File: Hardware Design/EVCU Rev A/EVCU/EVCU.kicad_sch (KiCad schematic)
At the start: 89 parts, among them J1 Conn_01x06, J2 Conn_01x02, J3 APPS/BSE_Conn, J4 Micro_SD_Card, J5 DB9_Male, J6 Conn_01x02, Q1 Q_PMOS_GSD, U1 AZ1117-3.3, U10 EMIF06-MSD02N16, U11 ESDALC6V1W5, U2 AP62250WU-7, U3 STM32L4R9ZITx, U4 LM358, U5 MPU-6500, U6 SN65HVD230, U7 LM358, U9 ESDCAN24-2BLY, X1 ECS-2520MV-160-CN-TR

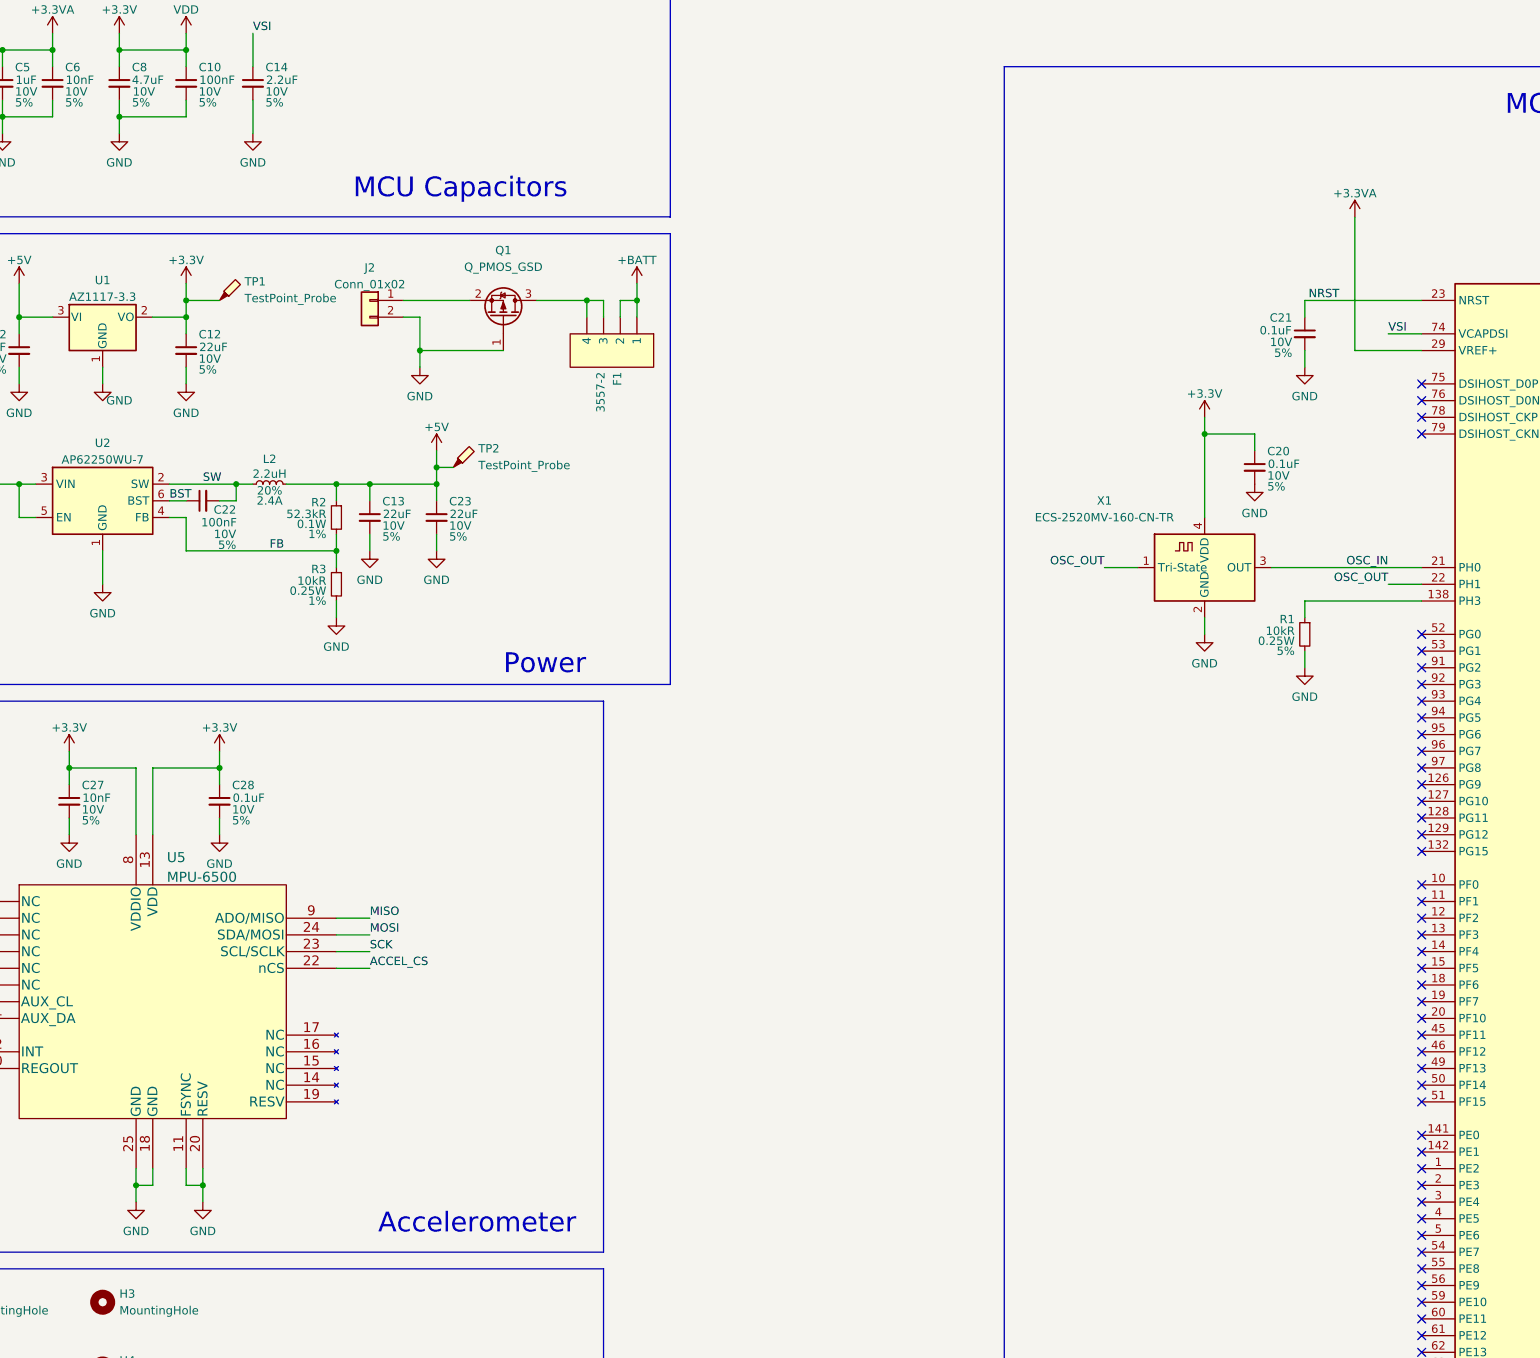
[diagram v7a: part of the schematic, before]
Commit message: added vref+ caps, fixed f1 via error, fixed gyro footprint, pcb ready for manufacturing
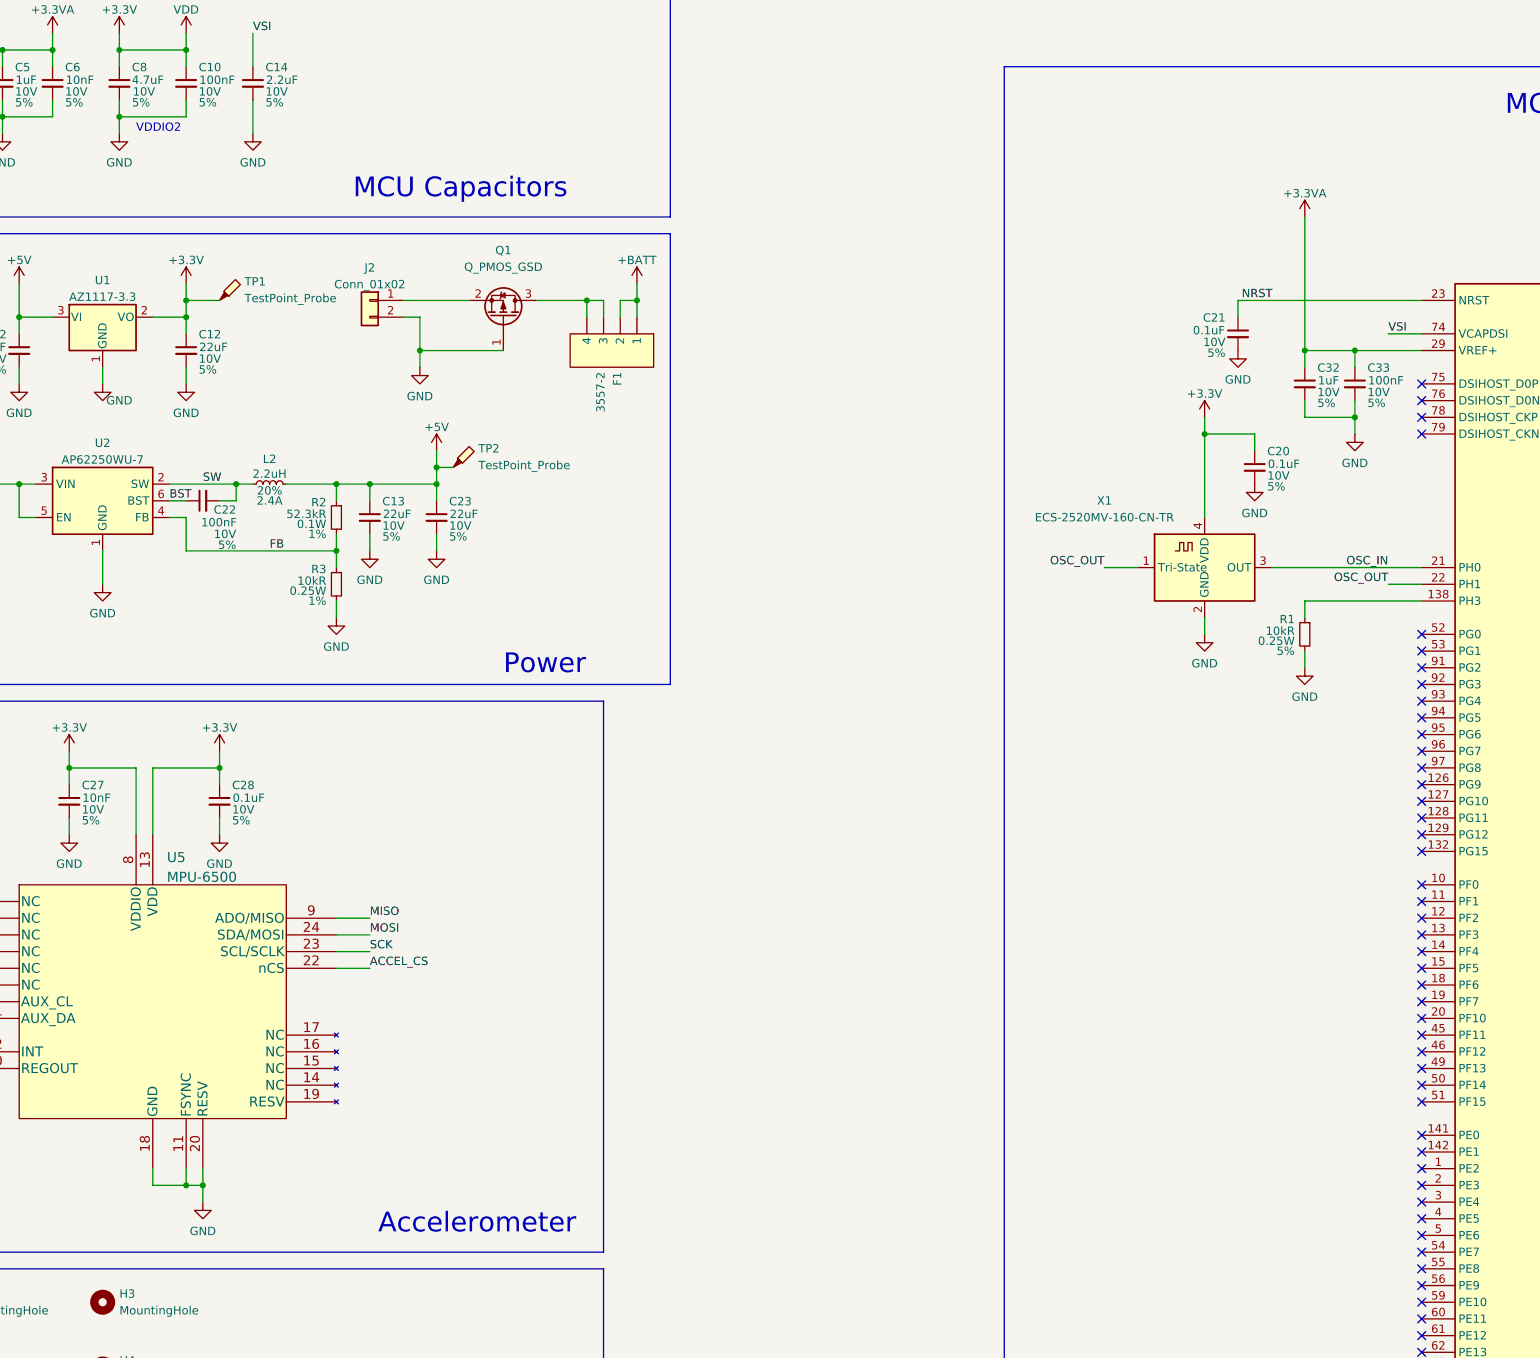
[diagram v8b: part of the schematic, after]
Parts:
- added C32: 1uF, Capacitor_SMD:C_0603_1608Metric_Pad1.08x0.95mm_HandSolder, symbol Device:C_Small
- added C33: 100nF, Capacitor_SMD:C_0603_1608Metric_Pad1.08x0.95mm_HandSolder, symbol Device:C_Small
- U5: footprint Package_DFN_QFN:QFN-24-3x3mm_P0.4mm_EP1.75x1.6mm -> Package_DFN_QFN:QFN-24_3x3mm_P0.4mm
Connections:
- net +3.3VA: now also C32.1, C33.1
- net GND: now also C32.2, C33.2; no longer U5.25 (GND)
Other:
- note added: "VDDIO2"
- moved on the sheet: C21
